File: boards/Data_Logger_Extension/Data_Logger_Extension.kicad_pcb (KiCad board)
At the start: 2 copper layers, 70 x 70 mm, 2 parts, among them J1 Data Logger, J2 micromatch_female_RA_20

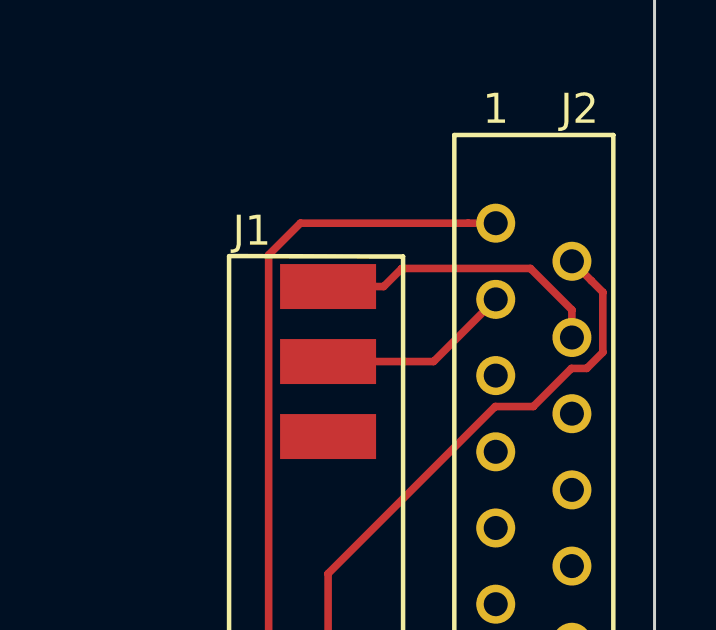
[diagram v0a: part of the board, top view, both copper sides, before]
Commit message: Fixed data logger.Can H/L
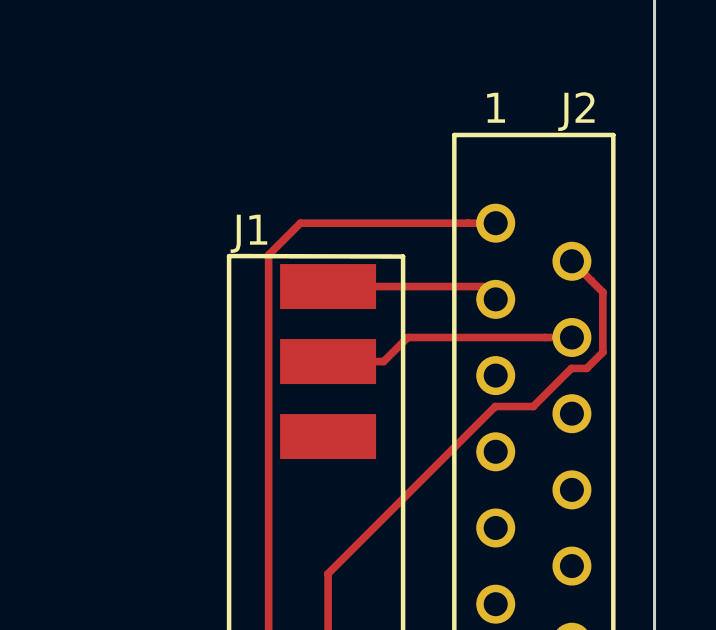
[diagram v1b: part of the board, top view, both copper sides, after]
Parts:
- J1: value Data Logger -> Ultrafit_5
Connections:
- J1 pad 1: /CAN_Low -> /CAN_High
- J1 pad 2: /CAN_High -> /CAN_Low
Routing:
- net /CAN_Low: track 9.87 -> 8.46 mm
- net /CAN_High: track 6.45 -> 5.77 mm
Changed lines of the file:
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@@
   (general
     (links 4)
-    (no_connects 4)
-    (area 95.009999 78.729999 167.191 148.830001)
+    (no_connects 2)
+    (area 95.009999 78.729999 165.110001 148.830001)
     (thickness 1.6)
     (drawings 13)
-    (tracks 22)
+    (tracks 21)
     (zones 0)
     (modules 2)
@@
     (add_net "Net-(J2-Pad9)")
   )
-  (module footprints:Data-Logger-Pads (layer F.Cu)
-    (at 154.178 103.458 270)
-    (fp_text reference J1 (at -1.858 2.54 360) (layer F.SilkS)
-      (effects (font (size 1 1) (thickness 0.15)))
-    )
-    (fp_text value "Data Logger" (at -2.62 9.906 360) (layer F.Fab)
-      (effects (font (size 1 1) (thickness 0.15)))
-    )
-    (fp_line (start -1.016 3.302) (end -1 -2.5) (layer F.SilkS) (width 0.15))
-    (fp_line (start 18 3.3) (end -1 3.3) (layer F.SilkS) (width 0.15))
-    (fp_line (start 18 -2.5) (end 18 3.3) (layer F.SilkS) (width 0.15))
-    (fp_line (start -1 -2.5) (end 18 -2.5) (layer F.SilkS) (width 0.15))
-    (pad 2 smd rect (at 2.5 0 270) (size 1.5 3.2) (layers F.Cu F.Paste F.Mask)
-      (net 1 /CAN_High))
-    (pad 1 smd rect (at 0 0 270) (size 1.5 3.2) (layers F.Cu F.Paste F.Mask)
-      (net 2 /CAN_Low))
-    (pad 4 smd rect (at 14.5 0 270) (size 1.5 3.2) (layers F.Cu F.Paste F.Mask)
-      (net 3 +5V))
-    (pad 3 smd rect (at 5 0 270) (size 1.5 3.2) (layers F.Cu F.Paste F.Mask)
-      (net 4 "Net-(J1-Pad3)"))
-    (pad 5 smd rect (at 17 0 270) (size 1.5 3.2) (layers F.Cu F.Paste F.Mask)
-      (net 5 GND))
-  )
   (module footprints:micromatch_female_ra_20 (layer F.Cu)
     (at 159.766 106.426)
@@
       (net 21 "Net-(J2-Pad20)"))
   )
+  (module footprints:Data-Logger-Pads (layer F.Cu)
+    (at 154.178 103.458 270)
+    (fp_text reference J1 (at -1.858 2.54 360) (layer F.SilkS)
+      (effects (font (size 1 1) (thickness 0.15)))
+    )
+    (fp_text value Ultrafit_5 (at -2.62 9.906 360) (layer F.Fab)
+      (effects (font (size 1 1) (thickness 0.15)))
+    )
+    (fp_line (start -1.016 3.302) (end -1 -2.5) (layer F.SilkS) (width 0.15))
+    (fp_line (start 18 3.3) (end -1 3.3) (layer F.SilkS) (width 0.15))
+    (fp_line (start 18 -2.5) (end 18 3.3) (layer F.SilkS) (width 0.15))
+    (fp_line (start -1 -2.5) (end 18 -2.5) (layer F.SilkS) (width 0.15))
+    (pad 2 smd rect (at 2.5 0 270) (size 1.5 3.2) (layers F.Cu F.Paste F.Mask)
+      (net 2 /CAN_Low))
+    (pad 1 smd rect (at 0 0 270) (size 1.5 3.2) (layers F.Cu F.Paste F.Mask)
+      (net 1 /CAN_High))
+    (pad 4 smd rect (at 14.5 0 270) (size 1.5 3.2) (layers F.Cu F.Paste F.Mask)
+      (net 3 +5V))
+    (pad 3 smd rect (at 5 0 270) (size 1.5 3.2) (layers F.Cu F.Paste F.Mask)
+      (net 4 "Net-(J1-Pad3)"))
+    (pad 5 smd rect (at 17 0 270) (size 1.5 3.2) (layers F.Cu F.Paste F.Mask)
+      (net 5 GND))
+  )
   (dimension 50.038645 (width 0.3) (layer F.SilkS)
     (gr_text "50.039 mm" (at 131.665961 96.16308 0.2908390224) (layer F.SilkS)
@@
   (gr_line (start 165.06 82.78) (end 165.06 144.78) (layer Edge.Cuts) (width 0.1))
   (gr_arc (start 99.06 144.78) (end 95.06 144.78) (angle -90) (layer Edge.Cuts) (width 0.1))
-  (segment (start 154.178 105.958) (end 157.694 105.958) (width 0.254) (layer F.Cu) (net 1))
-  (segment (start 157.694 105.958) (end 159.766 103.886) (width 0.254) (layer F.Cu) (net 1))
-  (segment (start 154.178 103.458) (end 156.032 103.458) (width 0.254) (layer F.Cu) (net 2))
-  (segment (start 156.635001 102.854999) (end 160.924237 102.854999) (width 0.254) (layer F.Cu) (net 2))
-  (segment (start 156.032 103.458) (end 156.635001 102.854999) (width 0.254) (layer F.Cu) (net 2))
-  (segment (start 160.924237 102.854999) (end 162.306 104.236762) (width 0.254) (layer F.Cu) (net 2))
-  (segment (start 162.306 104.236762) (end 162.306 105.156) (width 0.254) (layer F.Cu) (net 2))
+  (segment (start 154.178 103.458) (end 159.338 103.458) (width 0.254) (layer F.Cu) (net 1))
+  (segment (start 159.338 103.458) (end 159.766 103.886) (width 0.254) (layer F.Cu) (net 1))
+  (segment (start 154.178 105.958) (end 156.032 105.958) (width 0.254) (layer F.Cu) (net 2))
+  (segment (start 156.834 105.156) (end 161.386762 105.156) (width 0.254) (layer F.Cu) (net 2))
+  (segment (start 161.386762 105.156) (end 162.306 105.156) (width 0.254) (layer F.Cu) (net 2))
+  (segment (start 156.032 105.958) (end 156.834 105.156) (width 0.254) (layer F.Cu) (net 2))
   (segment (start 154.178 117.958) (end 154.178 113.028118) (width 0.254) (layer F.Cu) (net 3))
   (segment (start 154.178 113.028118) (end 159.749117 107.457001) (width 0.254) (layer F.Cu) (net 3))

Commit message: Modifed data-logger board
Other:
- board text added: "Data Logger Board Olin Electric Motorsports"
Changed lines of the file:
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@@
   (general
     (links 4)
-    (no_connects 2)
-    (area 95.009999 78.729999 165.110001 148.830001)
+    (no_connects 0)
+    (area 95.009999 78.729999 167.245 148.830001)
     (thickness 1.6)
     (drawings 13)
@@
     (visible_elements FFFFFF7F)
     (pcbplotparams
-      (layerselection 0x00030_80000001)
+      (layerselection 0x010f0_80000001)
       (usegerberextensions false)
       (excludeedgelayer true)
@@
       (outputformat 1)
       (mirror false)
-      (drillshape 1)
+      (drillshape 0)
       (scaleselection 1)
-      (outputdirectory ""))
+      (outputdirectory /home/corey/Desktop/Formula/MK_III-Boards/boards/Data_Logger_Extension/Rev1/Gerb/))
   )
   (net 0 "")
@@
       (net 5 GND))
   )
-  (dimension 50.038645 (width 0.3) (layer F.SilkS)
-    (gr_text "50.039 mm" (at 131.665961 96.16308 0.2908390224) (layer F.SilkS)
-      (effects (font (size 1.5 1.5) (thickness 0.3)))
-    )
-    (feature1 (pts (xy 156.702155 99.423168) (xy 156.678109 94.686098)))
-    (feature2 (pts (xy 106.664155 99.677168) (xy 106.640109 94.940098)))
-    (crossbar (pts (xy 106.653814 97.640063) (xy 156.691814 97.386063)))
-    (arrow1a (pts (xy 156.691814 97.386063) (xy 155.568301 97.978194)))
-    (arrow1b (pts (xy 156.691814 97.386063) (xy 155.562348 96.805368)))
-    (arrow2a (pts (xy 106.653814 97.640063) (xy 107.78328 98.220758)))
-    (arrow2b (pts (xy 106.653814 97.640063) (xy 107.777327 97.047932)))
+  (gr_text "Data Logger Board\nOlin Electric Motorsports" (at 103.886 83.82) (layer F.SilkS)
+    (effects (font (size 1.5 1.5) (thickness 0.3)) (justify left))
   )
   (gr_arc (start 161.06 144.78) (end 161.06 148.78) (angle -90) (layer Edge.Cuts) (width 0.1))

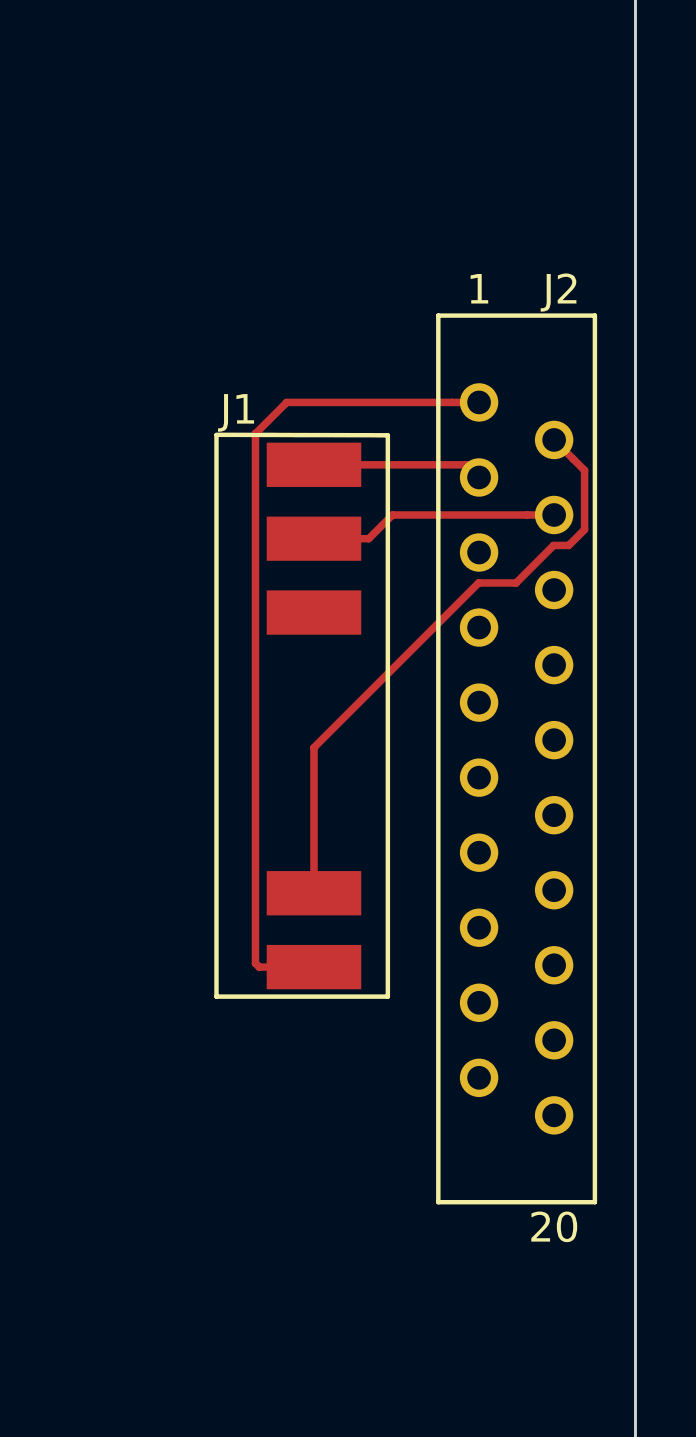
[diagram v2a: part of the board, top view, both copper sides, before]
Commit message: working on LV interface layout, added measurements to LV box boards to accurately place connectors
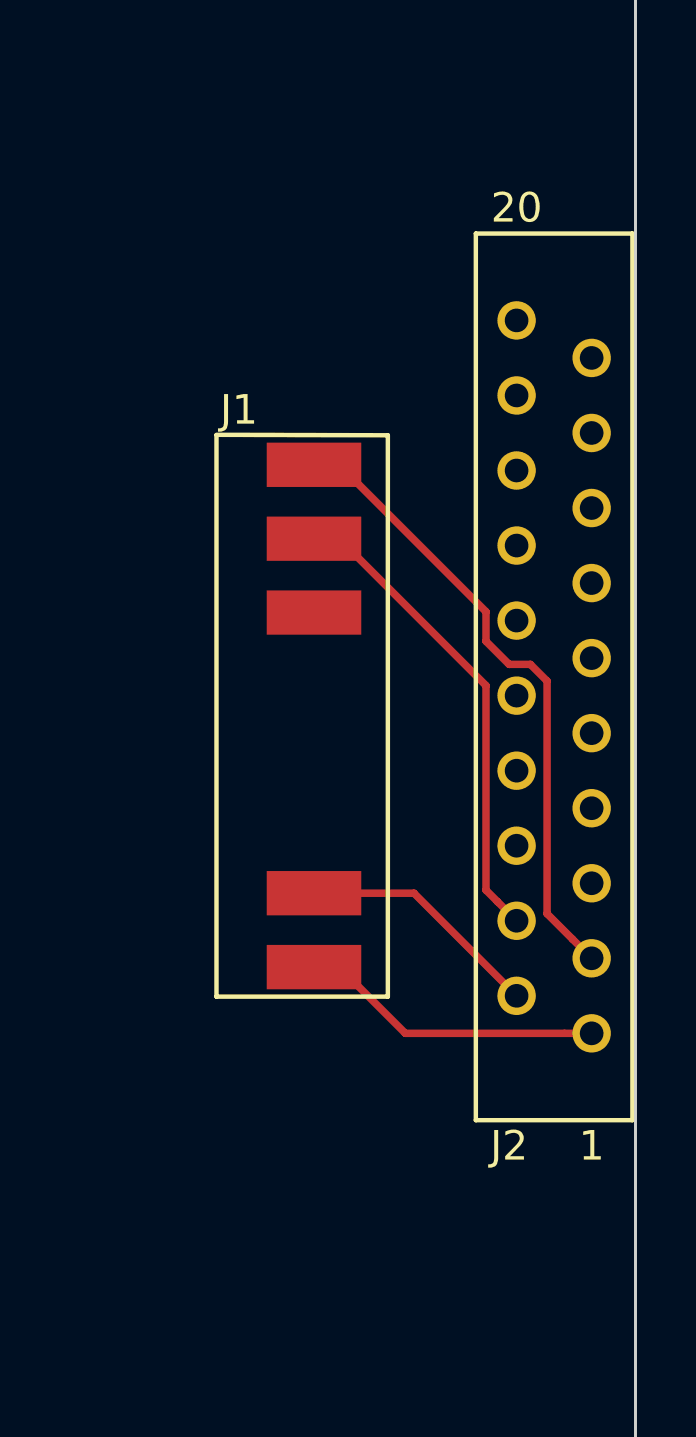
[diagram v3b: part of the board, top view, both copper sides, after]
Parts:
- moved J2 11.8 mm to (163.6, 117.6), turned to 180 degrees
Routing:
- net GND: track 28.0 -> 10.3 mm
- net /CAN_High: track 5.77 -> 21.5 mm
- net +5V: track 20.6 -> 8.30 mm
- net /CAN_Low: track 8.46 -> 16.3 mm
